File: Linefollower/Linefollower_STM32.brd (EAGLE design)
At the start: 97.8 x 86.4 mm, 63 parts, among them IC2 L298, IC4 STM32F101RET6, Q1 CSM-7X-DU

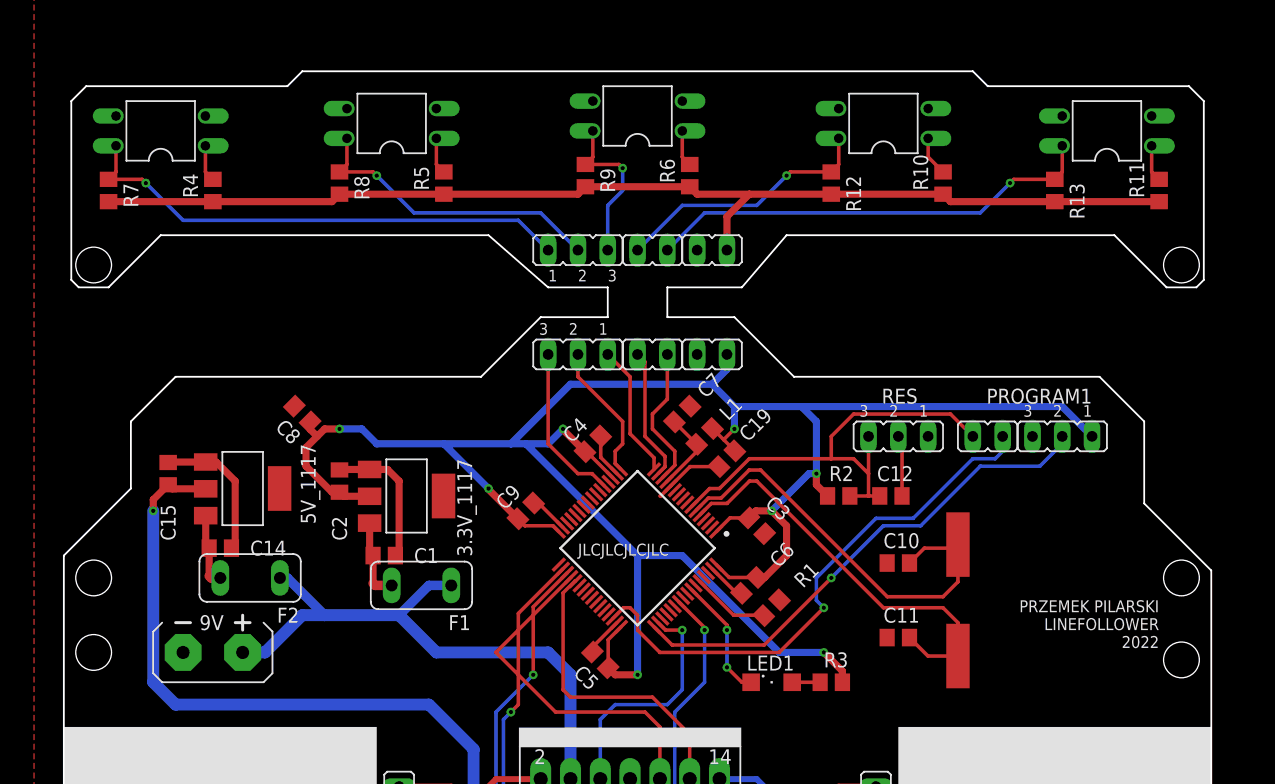
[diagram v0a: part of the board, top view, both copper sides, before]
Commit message: 6 sensor strip
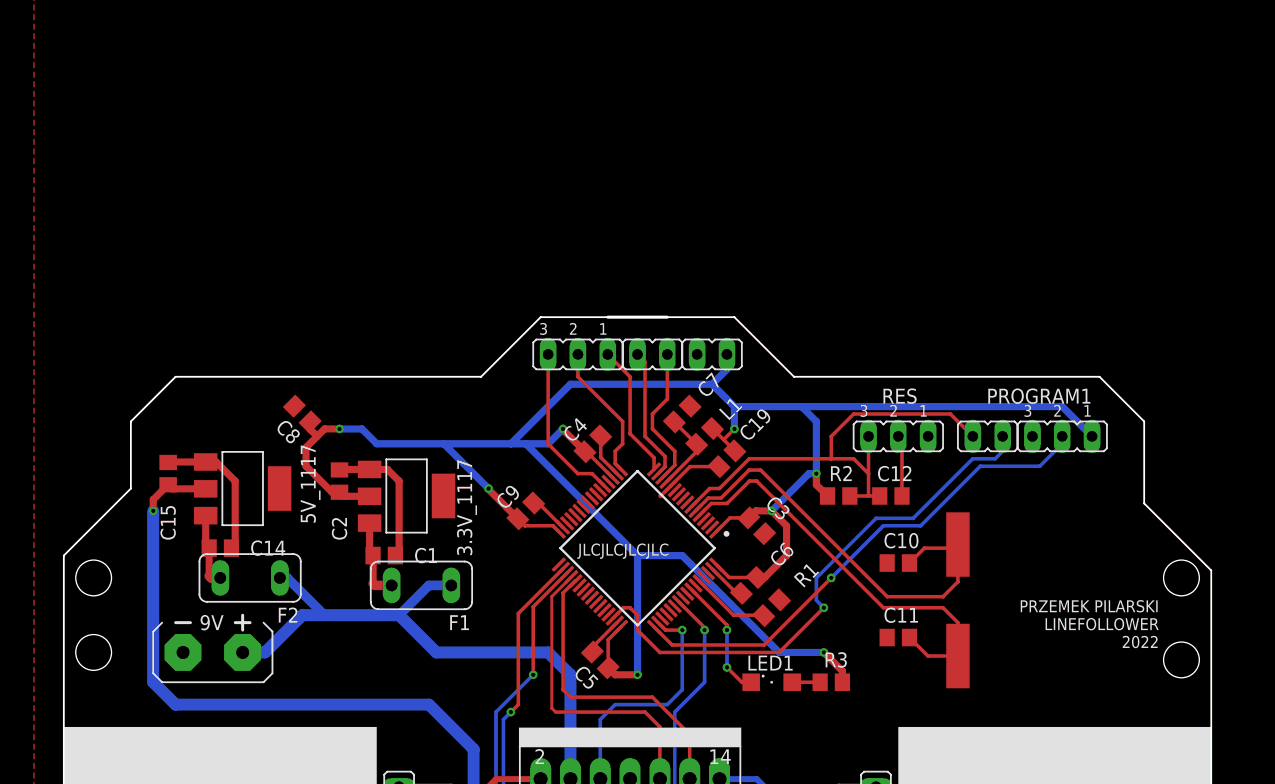
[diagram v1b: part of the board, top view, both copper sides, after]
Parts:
- removed 33GNDS, S4S5S: (no value), jumper:JP1
- removed DIODA-1, DIODA-2, DIODA-3, DIODA-4, DIODA-5: CNY70, optocoupler:DIL04
- removed R10, R11, R4, R5, R6: 100, rcl:R0805
- removed R12, R13, R7, R8, R9: 20k, rcl:R0805
- removed S1S2S3S: (no value), jumper:JP2
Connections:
- removed net N$10: DIODA-3.1, R6.2
- removed net N$11: DIODA-4.1, R10.2
- removed net N$14: DIODA-5.1, R11.2
- removed net N$8: DIODA-1.1, R4.2
- removed net N$9: DIODA-2.1, R5.2
- removed net S1: DIODA-1.4, IC4.21, R7.1, S1S2S3M.3, S1S2S3S.1
- removed net S5: DIODA-5.4, IC4.14, R13.1, S4S5M.1, S4S5S.2
- new net S$11: IC4.14, S4S5M.1
- new net S$7: IC4.21, S1S2S3M.3
- net 3.3V: no longer 33GNDS.1, R10.1, R11.1, R12.2, R13.2, R4.1, R5.1, R6.1, R7.2, R8.2, R9.2
- net GND: no longer 33GNDS.2, DIODA-1.2, DIODA-1.3, DIODA-2.2, DIODA-2.3, DIODA-3.2, DIODA-3.3, DIODA-4.2, DIODA-4.3, DIODA-5.2, DIODA-5.3
- net S2: no longer DIODA-2.4, R8.1, S1S2S3S.2
- net S3: no longer DIODA-3.4, R9.1, S1S2S3S.3
- net S4: no longer DIODA-4.4, R12.1, S4S5S.1
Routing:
- net 3.3V: track 294.2 -> 198.0 mm
- net S1: track 57.0 -> 0.00 mm, vias 1 -> 0
- net S5: track 50.9 -> 0.00 mm, vias 1 -> 0
- net S2: track 38.1 -> 11.8 mm, vias 1 -> 0
- net S4: track 33.8 -> 11.4 mm, vias 1 -> 0
- net S3: track 25.4 -> 11.4 mm, vias 1 -> 0
- net S$7: track 0.00 -> 13.9 mm
- net S$11: track 0.00 -> 12.3 mm
- net IN3: track 30.1 -> 26.2 mm
- net N$11: track 3.39 -> 0.00 mm
- net N$14: track 3.12 -> 0.00 mm
- net N$8: track 3.12 -> 0.00 mm
- net N$10: track 3.12 -> 0.00 mm
- net N$9: track 3.12 -> 0.00 mm
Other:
- board size 97.8 x 86.4 mm -> 97.8 x 65.4 mm
